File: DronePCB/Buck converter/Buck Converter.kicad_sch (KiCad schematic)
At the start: 8 parts, among them U1 LMR33630ADDA

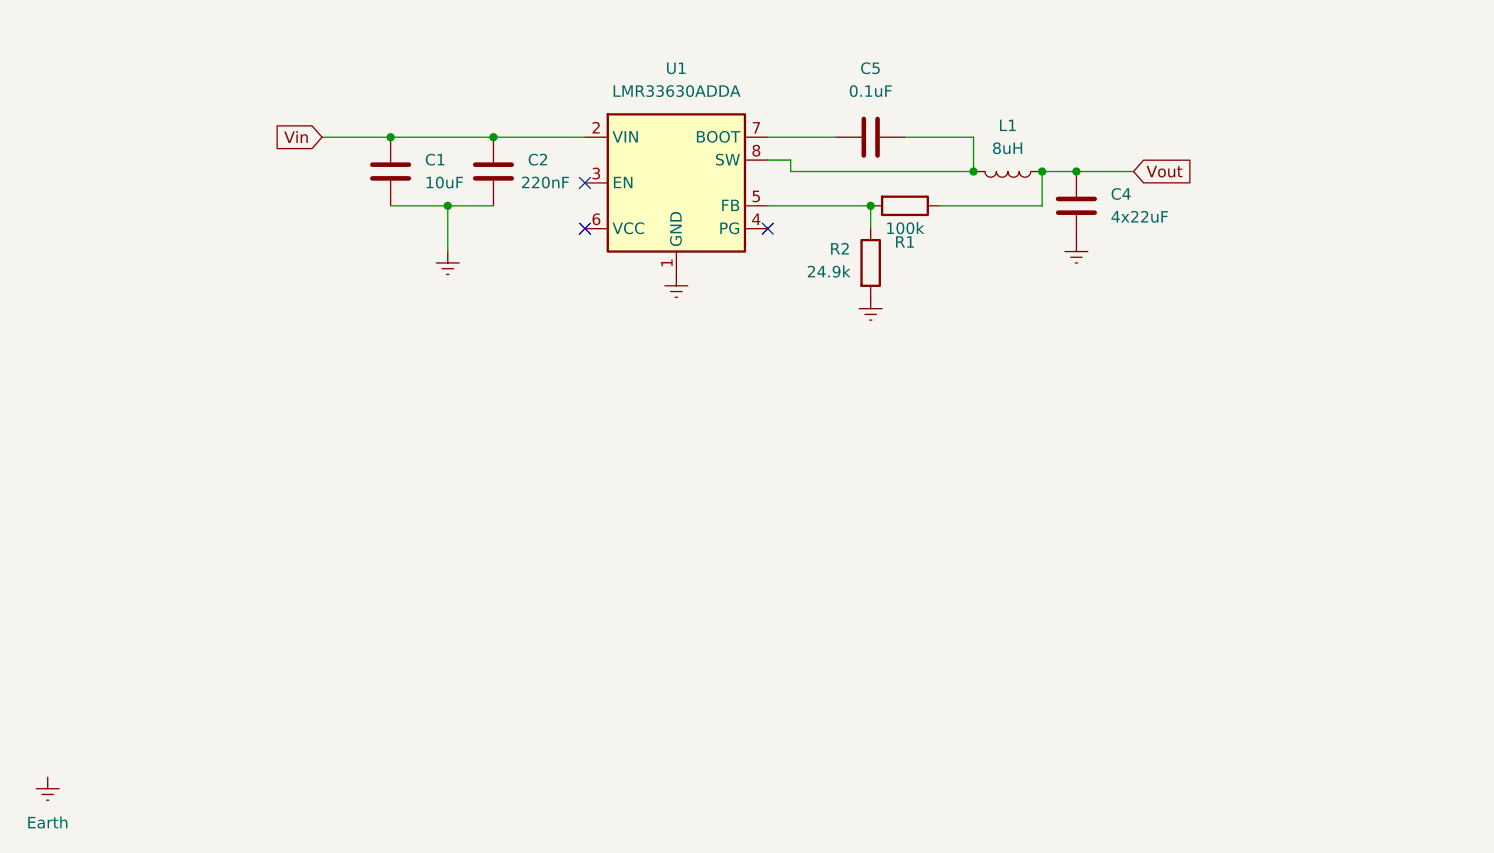
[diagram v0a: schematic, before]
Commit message: Added IR circuit to main schematic | fixed RPi header gnd
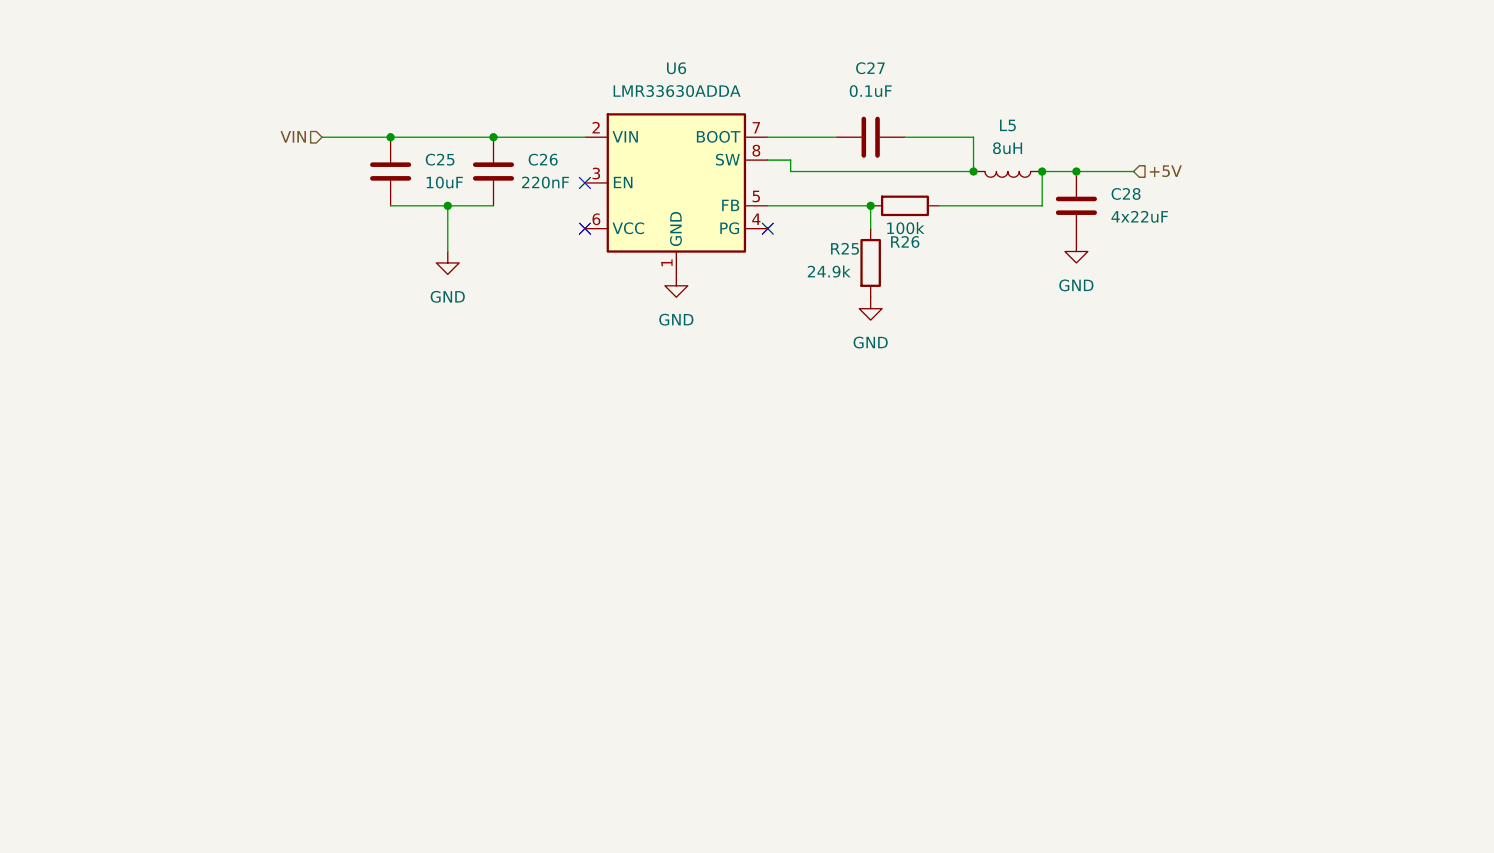
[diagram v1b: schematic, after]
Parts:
- renumbered C1 to C25, C2 to C26, C5 to C27, C4 to C28, L1 to L5, R2 to R25, R1 to R26, U1 to U6
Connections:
- net Earth renamed GND
- net Vin renamed VIN
- net Vout renamed +5V

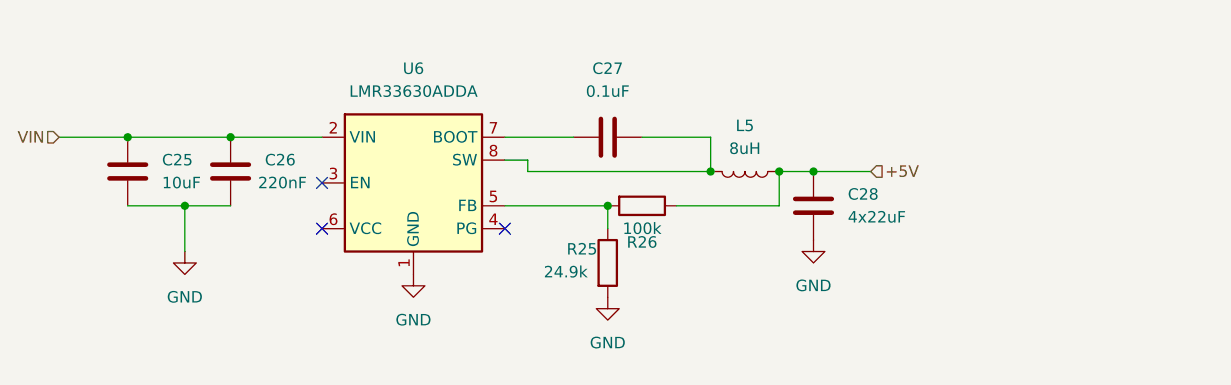
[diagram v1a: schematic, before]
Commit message: Completed H-Bridge Circuit | Finished Schematic | Working on pcb design
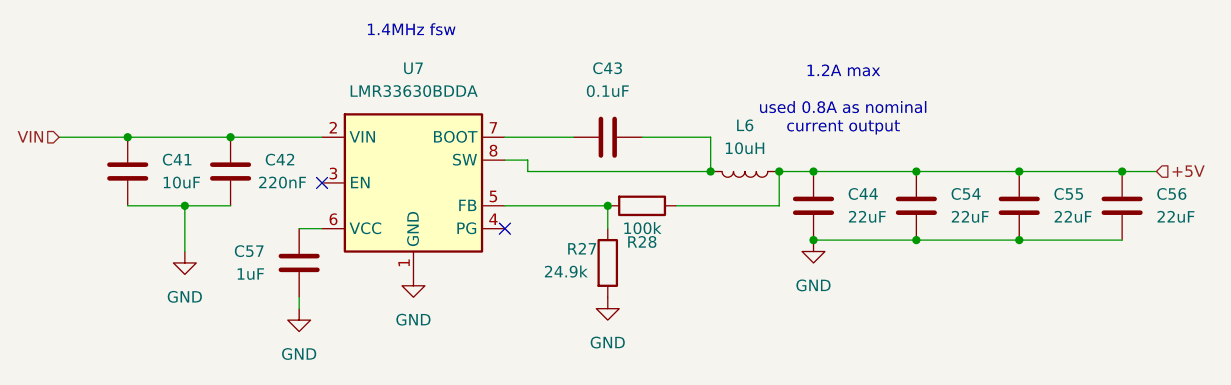
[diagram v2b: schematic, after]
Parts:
- added C54, C55, C56: 22uF, Capacitor_SMD:C_0603_1608Metric, symbol Device:C
- added C57: 1uF, Capacitor_SMD:C_0603_1608Metric, symbol Device:C
- C41: renamed from C25; footprint (none) -> Capacitor_SMD:C_0603_1608Metric
- C42: renamed from C26; footprint (none) -> Capacitor_SMD:C_0603_1608Metric
- C43: renamed from C27; footprint (none) -> Capacitor_SMD:C_0603_1608Metric
- C44: renamed from C28; value 4x22uF -> 22uF; footprint (none) -> Capacitor_SMD:C_0603_1608Metric
- L6: renamed from L5; value 8uH -> 10uH; footprint (none) -> Inductor_SMD:L_Taiyo-Yuden_NR-40xx
- R27: renamed from R25; footprint (none) -> Resistor_SMD:R_0603_1608Metric
- R28: renamed from R26; footprint (none) -> Resistor_SMD:R_0603_1608Metric
- U7: renamed from U6; value LMR33630ADDA -> LMR33630BDDA
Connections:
- net +5V: now also C54.1, C55.1, C56.1
- net GND: now also C54.2, C55.2, C56.2, C57.2
- net at U7.6 (VCC): now also C57.1
- no-connect marks 3 -> 2
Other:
- note added: "1.2A max used 0.8A as nominal current output"
- note added: "1.4MHz fsw"

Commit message: All circuits complete
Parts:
- C41: footprint Capacitor_SMD:C_0603_1608Metric -> Capacitor_SMD:C_1206_3216Metric
- renumbered C57 to C43, C43 to C44, C44 to C45, C54 to C46, C55 to C47, C56 to C48, R27 to R28, R28 to R29
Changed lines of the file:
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@@
 		(dnp no)
 		(fields_autoplaced yes)
-		(property "Reference" "C55"
+		(property "Reference" "C47"
 			(at 204.47 71.1199 0)
 			(show_name no)
@@
 			(project "DronePCB"
 				(path "/c9b74494-ac48-4f27-9459-39f0e04d9d05/a1c98057-a35a-4f76-997d-d93fb4728c5b"
-					(reference "C55")
+					(reference "C47")
 					(unit 1)
 				)
@@
 		(dnp no)
 		(fields_autoplaced yes)
-		(property "Reference" "#PWR068"
+		(property "Reference" "#PWR056"
 			(at 120.65 90.17 0)
 			(hide yes)
@@
 			(project "DronePCB"
 				(path "/c9b74494-ac48-4f27-9459-39f0e04d9d05/a1c98057-a35a-4f76-997d-d93fb4728c5b"
-					(reference "#PWR068")
+					(reference "#PWR056")
 					(unit 1)
 				)
@@
 		(dnp no)
 		(fields_autoplaced yes)
-		(property "Reference" "#PWR055"
+		(property "Reference" "#PWR057"
 			(at 133.35 86.36 0)
 			(hide yes)
@@
 			(project "DronePCB"
 				(path "/c9b74494-ac48-4f27-9459-39f0e04d9d05/a1c98057-a35a-4f76-997d-d93fb4728c5b"
-					(reference "#PWR055")
+					(reference "#PWR057")
 					(unit 1)
 				)
@@
 		(dnp no)
 		(fields_autoplaced yes)
-		(property "Reference" "C43"
+		(property "Reference" "C44"
 			(at 154.94 57.15 90)
 			(show_name no)
@@
 			(project "DronePCB"
 				(path "/c9b74494-ac48-4f27-9459-39f0e04d9d05/a1c98057-a35a-4f76-997d-d93fb4728c5b"
-					(reference "C43")
+					(reference "C44")
 					(unit 1)
 				)
@@
 		(in_pos_files yes)
 		(dnp no)
-		(property "Reference" "R27"
+		(property "Reference" "R28"
 			(at 150.368 77.216 0)
 			(show_name no)
@@
 			(project "DronePCB"
 				(path "/c9b74494-ac48-4f27-9459-39f0e04d9d05/a1c98057-a35a-4f76-997d-d93fb4728c5b"
-					(reference "R27")
+					(reference "R28")
 					(unit 1)
 				)
@@
 		(in_pos_files yes)
 		(dnp no)
-		(property "Reference" "C57"
+		(property "Reference" "C43"
 			(at 116.84 77.4699 0)
 			(show_name no)
@@
 			(project "DronePCB"
 				(path "/c9b74494-ac48-4f27-9459-39f0e04d9d05/a1c98057-a35a-4f76-997d-d93fb4728c5b"
-					(reference "C57")
+					(reference "C43")
 					(unit 1)
 				)
@@
 		(dnp no)
 		(fields_autoplaced yes)
-		(property "Reference" "#PWR054"
+		(property "Reference" "#PWR055"
 			(at 107.95 83.82 0)
 			(hide yes)
@@
 			(project "DronePCB"
 				(path "/c9b74494-ac48-4f27-9459-39f0e04d9d05/a1c98057-a35a-4f76-997d-d93fb4728c5b"
-					(reference "#PWR054")
+					(reference "#PWR055")
 					(unit 1)
 				)
@@
 		(dnp no)
 		(fields_autoplaced yes)
-		(property "Reference" "C44"
+		(property "Reference" "C45"
 			(at 181.61 71.1199 0)
 			(show_name no)
@@
 			(project "DronePCB"
 				(path "/c9b74494-ac48-4f27-9459-39f0e04d9d05/a1c98057-a35a-4f76-997d-d93fb4728c5b"
-					(reference "C44")
+					(reference "C45")
 					(unit 1)
 				)
@@
 		(in_pos_files yes)
 		(dnp no)
-		(property "Reference" "R28"
+		(property "Reference" "R29"
 			(at 158.75 76.454 90)
 			(show_name no)
@@
 			(project "DronePCB"
 				(path "/c9b74494-ac48-4f27-9459-39f0e04d9d05/a1c98057-a35a-4f76-997d-d93fb4728c5b"
-					(reference "R28")
+					(reference "R29")
 					(unit 1)
 				)
@@
 		(dnp no)
 		(fields_autoplaced yes)
-		(property "Reference" "#PWR056"
+		(property "Reference" "#PWR058"
 			(at 154.94 88.9 0)
 			(hide yes)
@@
 			(project "DronePCB"
 				(path "/c9b74494-ac48-4f27-9459-39f0e04d9d05/a1c98057-a35a-4f76-997d-d93fb4728c5b"
-					(reference "#PWR056")
+					(reference "#PWR058")
 					(unit 1)
 				)
@@
 		(dnp no)
 		(fields_autoplaced yes)
-		(property "Reference" "#PWR057"
+		(property "Reference" "#PWR059"
 			(at 177.8 82.55 0)
 			(hide yes)
@@
 			(project "DronePCB"
 				(path "/c9b74494-ac48-4f27-9459-39f0e04d9d05/a1c98057-a35a-4f76-997d-d93fb4728c5b"
-					(reference "#PWR057")
+					(reference "#PWR059")
 					(unit 1)
 				)
@@
 			)
 		)
-		(property "Footprint" "Capacitor_SMD:C_0603_1608Metric"
+		(property "Footprint" "Capacitor_SMD:C_1206_3216Metric"
 			(at 102.5652 72.39 0)
 			(hide yes)
@@
 		(dnp no)
 		(fields_autoplaced yes)
-		(property "Reference" "C54"
+		(property "Reference" "C46"
 			(at 193.04 71.1199 0)
 			(show_name no)
@@
 			(project "DronePCB"
 				(path "/c9b74494-ac48-4f27-9459-39f0e04d9d05/a1c98057-a35a-4f76-997d-d93fb4728c5b"
-					(reference "C54")
+					(reference "C46")
 					(unit 1)
 				)
@@
 		(dnp no)
 		(fields_autoplaced yes)
-		(property "Reference" "C56"
+		(property "Reference" "C48"
 			(at 215.9 71.1199 0)
 			(show_name no)
@@
 			(project "DronePCB"
 				(path "/c9b74494-ac48-4f27-9459-39f0e04d9d05/a1c98057-a35a-4f76-997d-d93fb4728c5b"
-					(reference "C56")
-					(unit 1)
-				)
+					(reference "C48")
+					(unit 1)
+				)
